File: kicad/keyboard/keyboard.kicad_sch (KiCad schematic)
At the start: 190 parts, among them J1 To main board J1, SW100 Esc, SW101 1 !, SW102 2 @, SW103 3 #, SW104 4 $, SW105 5 %, SW106 6 ^, SW107 7 &, SW110 8 *, SW111 9 (, SW112 0 ), SW113 - _, SW114 = +, SW115 Bksp, SW116 Tab, SW117 Q, SW120 W, SW121 E, SW122 R, SW123 T, SW124 Y, SW125 U, SW126 I, SW127 O, SW130 P, SW131 [ {, SW132 ] }, SW133 \ |, SW134 LCtrl, SW135 A, SW136 S, SW137 D, SW140 F, SW141 G, SW142 H, SW143 J, SW144 K, SW145 L, SW146 ; :, SW147 ' ", SW150 Enter, SW151 LShift, SW152 Z, SW153 X, SW154 C, SW155 V, SW156 B, SW157 N, SW160 M, SW161 , <, SW162 . >, SW163 / ?, SW164 RShift, SW165 Up, SW166 Caps, SW167 Fn, SW170 RAlt, SW171 LAlt, SW172 Space, SW173 RCtrl, SW175 Left, SW176 Down, SW177 Right

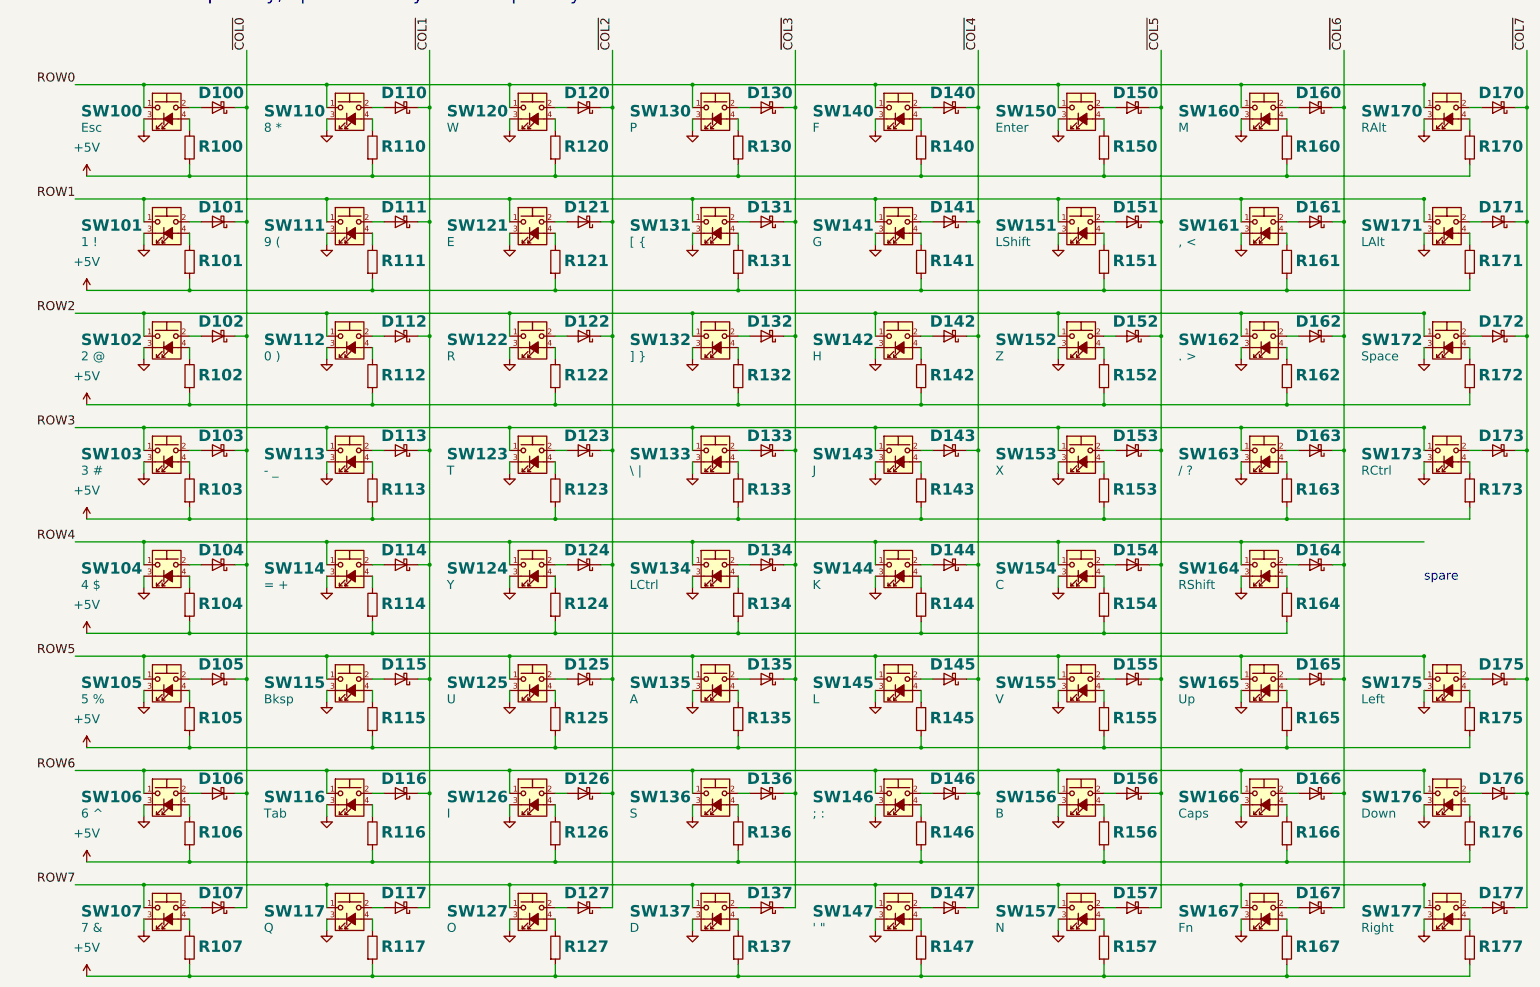
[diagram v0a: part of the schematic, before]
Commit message: Number parts from 1 for each kind; US zigzag resistor symbols
Main board R1-R54, RN1-RN2, D1-D5, JP1-JP2, F1, NT1, non-decoupling
capacitors C41-C46 (decaps keep Cn = Un); keyboard keys 1-63 row by row
(SWn, Dn, Rn per key). Resistors use R_US / R_Network08_US. --check now
fails on gaps or hundreds in the numbering. PDFs regenerated.

Co-Authored-By: Claude Opus 5.5 (1M context) <noreply@anthropic.com>
Claude-Session: https://claude.ai/code/session_01L9AkLuEg13EebxDmgXsaEp
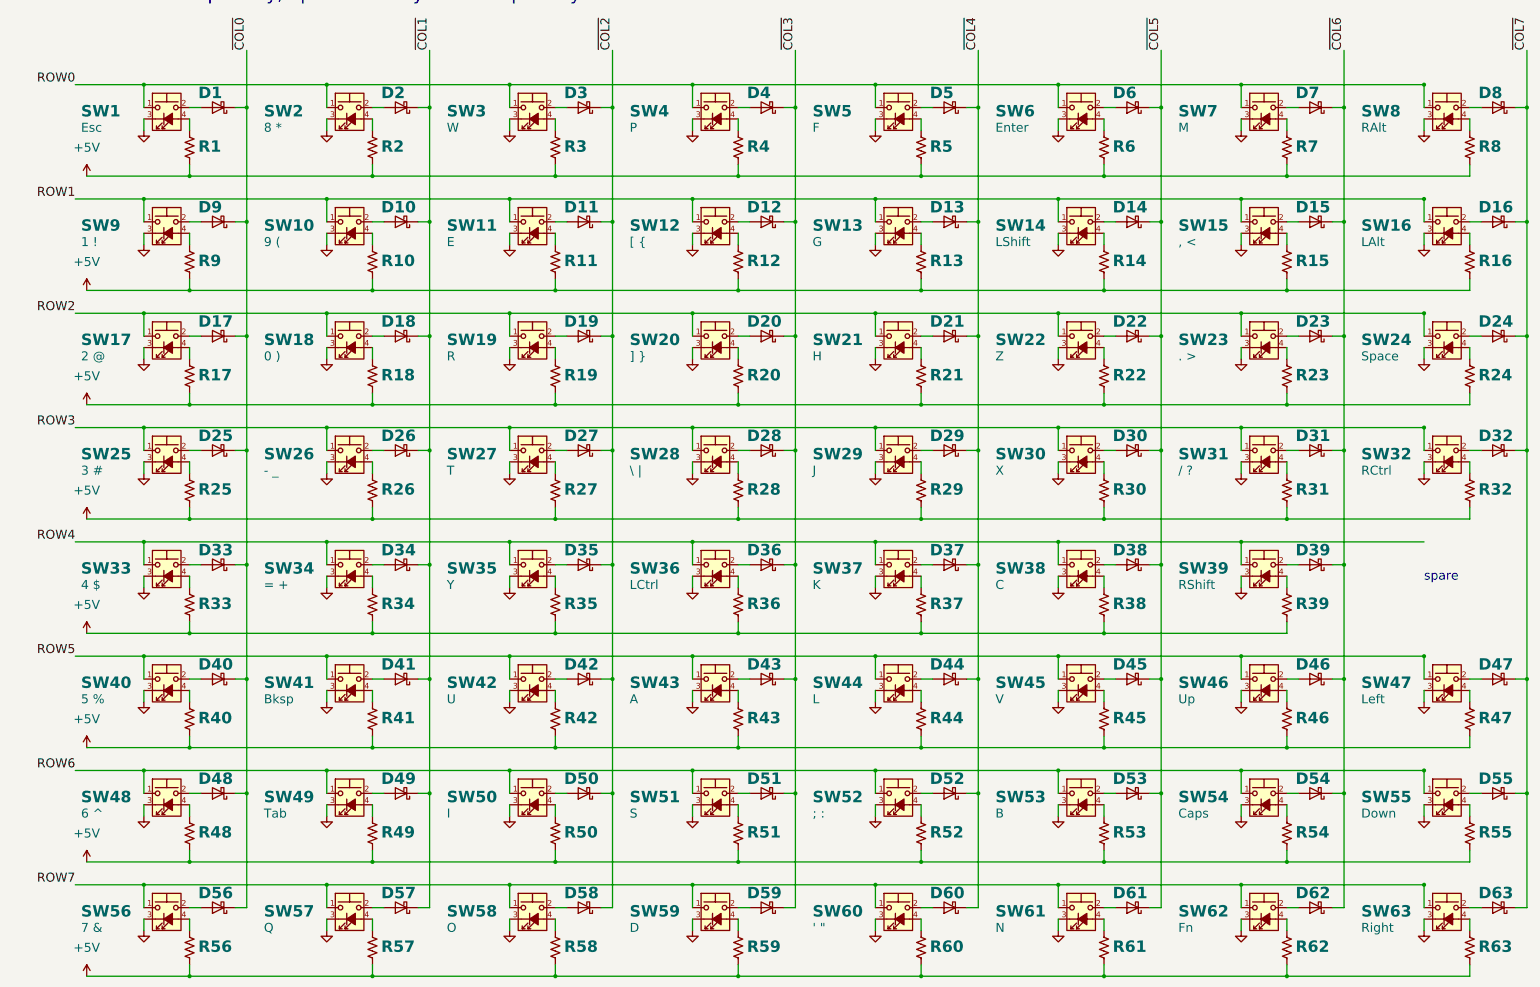
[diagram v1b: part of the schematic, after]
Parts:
- removed D100, D101, D102, D103, D104, D105, D106, D107, D110, D111, D112, D113, D114, D115, D116, D117, D120, D121, D122, D123, D124, D125, D126, D127, D130, D131, D132, D133, D134, D135, D136, D137, D140, D141, D142, D143, D144, D145, D146, D147, D150, D151, D152, D153, D154, D155, D156, D157, D160, D161, D162, D163, D164, D165, D166, D167, D170, D171, D172, D173, D175, D176, D177: BAT85, Diode_THT:D_DO-35_SOD27_P7.62mm_Horizontal, symbol placard_std:D_Schottky
- removed R100, R101, R102, R103, R104, R105, R106, R107, R110, R111, R112, R113, R114, R115, R116, R117, R120, R121, R122, R123, R124, R125, R126, R127, R130, R131, R132, R133, R134, R135, R136, R137, R140, R141, R142, R143, R144, R145, R146, R147, R150, R151, R152, R153, R154, R155, R156, R157, R160, R161, R162, R163, R164, R165, R166, R167, R170, R171, R172, R173, R175, R176, R177: 1k, Resistor_THT:R_Axial_DIN0207_L6.3mm_D2.5mm_P10.16mm_Horizontal, symbol placard_std:R
- removed SW100: Esc, placard:SW_Cherry_MX_LED_1.00u_PCB, symbol Switch:SW_Push_LED
- removed SW101: 1 !, placard:SW_Cherry_MX_LED_1.00u_PCB, symbol Switch:SW_Push_LED
- removed SW102: 2 @, placard:SW_Cherry_MX_LED_1.00u_PCB, symbol Switch:SW_Push_LED
- removed SW103: 3 #, placard:SW_Cherry_MX_LED_1.00u_PCB, symbol Switch:SW_Push_LED
- removed SW104: 4 $, placard:SW_Cherry_MX_LED_1.00u_PCB, symbol Switch:SW_Push_LED
- removed SW105: 5 %, placard:SW_Cherry_MX_LED_1.00u_PCB, symbol Switch:SW_Push_LED
- removed SW106: 6 ^, placard:SW_Cherry_MX_LED_1.00u_PCB, symbol Switch:SW_Push_LED
- removed SW107: 7 &, placard:SW_Cherry_MX_LED_1.00u_PCB, symbol Switch:SW_Push_LED
- removed SW110: 8 *, placard:SW_Cherry_MX_LED_1.00u_PCB, symbol Switch:SW_Push_LED
- removed SW111: 9 (, placard:SW_Cherry_MX_LED_1.00u_PCB, symbol Switch:SW_Push_LED
- removed SW112: 0 ), placard:SW_Cherry_MX_LED_1.00u_PCB, symbol Switch:SW_Push_LED
- removed SW113: - _, placard:SW_Cherry_MX_LED_1.00u_PCB, symbol Switch:SW_Push_LED
- removed SW114: = +, placard:SW_Cherry_MX_LED_1.00u_PCB, symbol Switch:SW_Push_LED
- removed SW115: Bksp, placard:SW_Cherry_MX_LED_2.00u_PCB, symbol Switch:SW_Push_LED
- removed SW116: Tab, placard:SW_Cherry_MX_LED_1.50u_PCB, symbol Switch:SW_Push_LED
- removed SW117: Q, placard:SW_Cherry_MX_LED_1.00u_PCB, symbol Switch:SW_Push_LED
- removed SW120: W, placard:SW_Cherry_MX_LED_1.00u_PCB, symbol Switch:SW_Push_LED
- removed SW121: E, placard:SW_Cherry_MX_LED_1.00u_PCB, symbol Switch:SW_Push_LED
- removed SW122: R, placard:SW_Cherry_MX_LED_1.00u_PCB, symbol Switch:SW_Push_LED
- removed SW123: T, placard:SW_Cherry_MX_LED_1.00u_PCB, symbol Switch:SW_Push_LED
- removed SW124: Y, placard:SW_Cherry_MX_LED_1.00u_PCB, symbol Switch:SW_Push_LED
- removed SW125: U, placard:SW_Cherry_MX_LED_1.00u_PCB, symbol Switch:SW_Push_LED
- removed SW126: I, placard:SW_Cherry_MX_LED_1.00u_PCB, symbol Switch:SW_Push_LED
- removed SW127: O, placard:SW_Cherry_MX_LED_1.00u_PCB, symbol Switch:SW_Push_LED
- removed SW130: P, placard:SW_Cherry_MX_LED_1.00u_PCB, symbol Switch:SW_Push_LED
- removed SW131: [ {, placard:SW_Cherry_MX_LED_1.00u_PCB, symbol Switch:SW_Push_LED
- removed SW132: ] }, placard:SW_Cherry_MX_LED_1.00u_PCB, symbol Switch:SW_Push_LED
- removed SW133: \ |, placard:SW_Cherry_MX_LED_1.50u_PCB, symbol Switch:SW_Push_LED
- removed SW134: LCtrl, placard:SW_Cherry_MX_LED_1.25u_PCB, symbol Switch:SW_Push_LED
- removed SW135: A, placard:SW_Cherry_MX_LED_1.00u_PCB, symbol Switch:SW_Push_LED
- removed SW136: S, placard:SW_Cherry_MX_LED_1.00u_PCB, symbol Switch:SW_Push_LED
- removed SW137: D, placard:SW_Cherry_MX_LED_1.00u_PCB, symbol Switch:SW_Push_LED
- removed SW140: F, placard:SW_Cherry_MX_LED_1.00u_PCB, symbol Switch:SW_Push_LED
- removed SW141: G, placard:SW_Cherry_MX_LED_1.00u_PCB, symbol Switch:SW_Push_LED
- removed SW142: H, placard:SW_Cherry_MX_LED_1.00u_PCB, symbol Switch:SW_Push_LED
- removed SW143: J, placard:SW_Cherry_MX_LED_1.00u_PCB, symbol Switch:SW_Push_LED
- removed SW144: K, placard:SW_Cherry_MX_LED_1.00u_PCB, symbol Switch:SW_Push_LED
- removed SW145: L, placard:SW_Cherry_MX_LED_1.00u_PCB, symbol Switch:SW_Push_LED
- removed SW146: ; :, placard:SW_Cherry_MX_LED_1.00u_PCB, symbol Switch:SW_Push_LED
- removed SW147: ' ", placard:SW_Cherry_MX_LED_1.00u_PCB, symbol Switch:SW_Push_LED
- removed SW150: Enter, placard:SW_Cherry_MX_LED_2.25u_PCB, symbol Switch:SW_Push_LED
- removed SW151: LShift, placard:SW_Cherry_MX_LED_2.25u_PCB, symbol Switch:SW_Push_LED
- removed SW152: Z, placard:SW_Cherry_MX_LED_1.00u_PCB, symbol Switch:SW_Push_LED
- removed SW153: X, placard:SW_Cherry_MX_LED_1.00u_PCB, symbol Switch:SW_Push_LED
- removed SW154: C, placard:SW_Cherry_MX_LED_1.00u_PCB, symbol Switch:SW_Push_LED
- removed SW155: V, placard:SW_Cherry_MX_LED_1.00u_PCB, symbol Switch:SW_Push_LED
- removed SW156: B, placard:SW_Cherry_MX_LED_1.00u_PCB, symbol Switch:SW_Push_LED
- removed SW157: N, placard:SW_Cherry_MX_LED_1.00u_PCB, symbol Switch:SW_Push_LED
- removed SW160: M, placard:SW_Cherry_MX_LED_1.00u_PCB, symbol Switch:SW_Push_LED
- removed SW161: , <, placard:SW_Cherry_MX_LED_1.00u_PCB, symbol Switch:SW_Push_LED
- removed SW162: . >, placard:SW_Cherry_MX_LED_1.00u_PCB, symbol Switch:SW_Push_LED
- removed SW163: / ?, placard:SW_Cherry_MX_LED_1.00u_PCB, symbol Switch:SW_Push_LED
- removed SW164: RShift, placard:SW_Cherry_MX_LED_1.75u_PCB, symbol Switch:SW_Push_LED
- removed SW165: Up, placard:SW_Cherry_MX_LED_1.00u_PCB, symbol Switch:SW_Push_LED
- removed SW166: Caps, placard:SW_Cherry_MX_LED_1.75u_PCB, symbol Switch:SW_Push_LED
- removed SW167: Fn, placard:SW_Cherry_MX_LED_1.25u_PCB, symbol Switch:SW_Push_LED
- removed SW170: RAlt, placard:SW_Cherry_MX_LED_1.00u_PCB, symbol Switch:SW_Push_LED
- removed SW171: LAlt, placard:SW_Cherry_MX_LED_1.25u_PCB, symbol Switch:SW_Push_LED
- removed SW172: Space, placard:SW_Cherry_MX_LED_6.25u_PCB, symbol Switch:SW_Push_LED
- removed SW173: RCtrl, placard:SW_Cherry_MX_LED_1.00u_PCB, symbol Switch:SW_Push_LED
- removed SW175: Left, placard:SW_Cherry_MX_LED_1.00u_PCB, symbol Switch:SW_Push_LED
- removed SW176: Down, placard:SW_Cherry_MX_LED_1.00u_PCB, symbol Switch:SW_Push_LED
- removed SW177: Right, placard:SW_Cherry_MX_LED_1.00u_PCB, symbol Switch:SW_Push_LED
- added D1, D10, D11, D12, D13, D14, D15, D16, D17, D18, D19, D2, D20, D21, D22, D23, D24, D25, D26, D27, D28, D29, D3, D30, D31, D32, D33, D34, D35, D36, D37, D38, D39, D4, D40, D41, D42, D43, D44, D45, D46, D47, D48, D49, D5, D50, D51, D52, D53, D54, D55, D56, D57, D58, D59, D6, D60, D61, D62, D63, D7, D8, D9: BAT85, Diode_THT:D_DO-35_SOD27_P7.62mm_Horizontal, symbol placard_std:D_Schottky
- added R1, R10, R11, R12, R13, R14, R15, R16, R17, R18, R19, R2, R20, R21, R22, R23, R24, R25, R26, R27, R28, R29, R3, R30, R31, R32, R33, R34, R35, R36, R37, R38, R39, R4, R40, R41, R42, R43, R44, R45, R46, R47, R48, R49, R5, R50, R51, R52, R53, R54, R55, R56, R57, R58, R59, R6, R60, R61, R62, R63, R7, R8, R9: 1k, Resistor_THT:R_Axial_DIN0207_L6.3mm_D2.5mm_P10.16mm_Horizontal, symbol placard_std:R_US
- added SW1: Esc, placard:SW_Cherry_MX_LED_1.00u_PCB, symbol Switch:SW_Push_LED
- added SW10: 9 (, placard:SW_Cherry_MX_LED_1.00u_PCB, symbol Switch:SW_Push_LED
- added SW11: E, placard:SW_Cherry_MX_LED_1.00u_PCB, symbol Switch:SW_Push_LED
- added SW12: [ {, placard:SW_Cherry_MX_LED_1.00u_PCB, symbol Switch:SW_Push_LED
- added SW13: G, placard:SW_Cherry_MX_LED_1.00u_PCB, symbol Switch:SW_Push_LED
- added SW14: LShift, placard:SW_Cherry_MX_LED_2.25u_PCB, symbol Switch:SW_Push_LED
- added SW15: , <, placard:SW_Cherry_MX_LED_1.00u_PCB, symbol Switch:SW_Push_LED
- added SW16: LAlt, placard:SW_Cherry_MX_LED_1.25u_PCB, symbol Switch:SW_Push_LED
- added SW17: 2 @, placard:SW_Cherry_MX_LED_1.00u_PCB, symbol Switch:SW_Push_LED
- added SW18: 0 ), placard:SW_Cherry_MX_LED_1.00u_PCB, symbol Switch:SW_Push_LED
- added SW19: R, placard:SW_Cherry_MX_LED_1.00u_PCB, symbol Switch:SW_Push_LED
- added SW2: 8 *, placard:SW_Cherry_MX_LED_1.00u_PCB, symbol Switch:SW_Push_LED
- added SW20: ] }, placard:SW_Cherry_MX_LED_1.00u_PCB, symbol Switch:SW_Push_LED
- added SW21: H, placard:SW_Cherry_MX_LED_1.00u_PCB, symbol Switch:SW_Push_LED
- added SW22: Z, placard:SW_Cherry_MX_LED_1.00u_PCB, symbol Switch:SW_Push_LED
- added SW23: . >, placard:SW_Cherry_MX_LED_1.00u_PCB, symbol Switch:SW_Push_LED
- added SW24: Space, placard:SW_Cherry_MX_LED_6.25u_PCB, symbol Switch:SW_Push_LED
- added SW25: 3 #, placard:SW_Cherry_MX_LED_1.00u_PCB, symbol Switch:SW_Push_LED
- added SW26: - _, placard:SW_Cherry_MX_LED_1.00u_PCB, symbol Switch:SW_Push_LED
- added SW27: T, placard:SW_Cherry_MX_LED_1.00u_PCB, symbol Switch:SW_Push_LED
- added SW28: \ |, placard:SW_Cherry_MX_LED_1.50u_PCB, symbol Switch:SW_Push_LED
- added SW29: J, placard:SW_Cherry_MX_LED_1.00u_PCB, symbol Switch:SW_Push_LED
- added SW3: W, placard:SW_Cherry_MX_LED_1.00u_PCB, symbol Switch:SW_Push_LED
- added SW30: X, placard:SW_Cherry_MX_LED_1.00u_PCB, symbol Switch:SW_Push_LED
- added SW31: / ?, placard:SW_Cherry_MX_LED_1.00u_PCB, symbol Switch:SW_Push_LED
- added SW32: RCtrl, placard:SW_Cherry_MX_LED_1.00u_PCB, symbol Switch:SW_Push_LED
- added SW33: 4 $, placard:SW_Cherry_MX_LED_1.00u_PCB, symbol Switch:SW_Push_LED
- added SW34: = +, placard:SW_Cherry_MX_LED_1.00u_PCB, symbol Switch:SW_Push_LED
- added SW35: Y, placard:SW_Cherry_MX_LED_1.00u_PCB, symbol Switch:SW_Push_LED
- added SW36: LCtrl, placard:SW_Cherry_MX_LED_1.25u_PCB, symbol Switch:SW_Push_LED
- added SW37: K, placard:SW_Cherry_MX_LED_1.00u_PCB, symbol Switch:SW_Push_LED
- added SW38: C, placard:SW_Cherry_MX_LED_1.00u_PCB, symbol Switch:SW_Push_LED
- added SW39: RShift, placard:SW_Cherry_MX_LED_1.75u_PCB, symbol Switch:SW_Push_LED
- added SW4: P, placard:SW_Cherry_MX_LED_1.00u_PCB, symbol Switch:SW_Push_LED
- added SW40: 5 %, placard:SW_Cherry_MX_LED_1.00u_PCB, symbol Switch:SW_Push_LED
- added SW41: Bksp, placard:SW_Cherry_MX_LED_2.00u_PCB, symbol Switch:SW_Push_LED
- added SW42: U, placard:SW_Cherry_MX_LED_1.00u_PCB, symbol Switch:SW_Push_LED
- added SW43: A, placard:SW_Cherry_MX_LED_1.00u_PCB, symbol Switch:SW_Push_LED
- added SW44: L, placard:SW_Cherry_MX_LED_1.00u_PCB, symbol Switch:SW_Push_LED
- added SW45: V, placard:SW_Cherry_MX_LED_1.00u_PCB, symbol Switch:SW_Push_LED
- added SW46: Up, placard:SW_Cherry_MX_LED_1.00u_PCB, symbol Switch:SW_Push_LED
- added SW47: Left, placard:SW_Cherry_MX_LED_1.00u_PCB, symbol Switch:SW_Push_LED
- added SW48: 6 ^, placard:SW_Cherry_MX_LED_1.00u_PCB, symbol Switch:SW_Push_LED
- added SW49: Tab, placard:SW_Cherry_MX_LED_1.50u_PCB, symbol Switch:SW_Push_LED
- added SW5: F, placard:SW_Cherry_MX_LED_1.00u_PCB, symbol Switch:SW_Push_LED
- added SW50: I, placard:SW_Cherry_MX_LED_1.00u_PCB, symbol Switch:SW_Push_LED
- added SW51: S, placard:SW_Cherry_MX_LED_1.00u_PCB, symbol Switch:SW_Push_LED
- added SW52: ; :, placard:SW_Cherry_MX_LED_1.00u_PCB, symbol Switch:SW_Push_LED
- added SW53: B, placard:SW_Cherry_MX_LED_1.00u_PCB, symbol Switch:SW_Push_LED
- added SW54: Caps, placard:SW_Cherry_MX_LED_1.75u_PCB, symbol Switch:SW_Push_LED
- added SW55: Down, placard:SW_Cherry_MX_LED_1.00u_PCB, symbol Switch:SW_Push_LED
- added SW56: 7 &, placard:SW_Cherry_MX_LED_1.00u_PCB, symbol Switch:SW_Push_LED
- added SW57: Q, placard:SW_Cherry_MX_LED_1.00u_PCB, symbol Switch:SW_Push_LED
- added SW58: O, placard:SW_Cherry_MX_LED_1.00u_PCB, symbol Switch:SW_Push_LED
- added SW59: D, placard:SW_Cherry_MX_LED_1.00u_PCB, symbol Switch:SW_Push_LED
- added SW6: Enter, placard:SW_Cherry_MX_LED_2.25u_PCB, symbol Switch:SW_Push_LED
- added SW60: ' ", placard:SW_Cherry_MX_LED_1.00u_PCB, symbol Switch:SW_Push_LED
- added SW61: N, placard:SW_Cherry_MX_LED_1.00u_PCB, symbol Switch:SW_Push_LED
- added SW62: Fn, placard:SW_Cherry_MX_LED_1.25u_PCB, symbol Switch:SW_Push_LED
- added SW63: Right, placard:SW_Cherry_MX_LED_1.00u_PCB, symbol Switch:SW_Push_LED
- added SW7: M, placard:SW_Cherry_MX_LED_1.00u_PCB, symbol Switch:SW_Push_LED
- added SW8: RAlt, placard:SW_Cherry_MX_LED_1.00u_PCB, symbol Switch:SW_Push_LED
- added SW9: 1 !, placard:SW_Cherry_MX_LED_1.00u_PCB, symbol Switch:SW_Push_LED
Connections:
- net +5V: now also R1.2, R10.2, R11.2, R12.2, R13.2, R14.2, R15.2, R16.2, R17.2, R18.2, R19.2, R2.2, R20.2, R21.2, R22.2, R23.2, R24.2, R25.2, R26.2, R27.2, R28.2, R29.2, R3.2, R30.2, R31.2, R32.2, R33.2, R34.2, R35.2, R36.2, R37.2, R38.2, R39.2, R4.2, R40.2, R41.2, R42.2, R43.2, R44.2, R45.2, R46.2, R47.2, R48.2, R49.2, R5.2, R50.2, R51.2, R52.2, R53.2, R54.2, R55.2, R56.2, R57.2, R58.2, R59.2, R6.2, R60.2, R61.2, R62.2, R63.2, R7.2, R8.2, R9.2
- net GND: now also SW1.3 (K), SW10.3 (K), SW11.3 (K), SW12.3 (K), SW13.3 (K), SW14.3 (K), SW15.3 (K), SW16.3 (K), SW17.3 (K), SW18.3 (K), SW19.3 (K), SW2.3 (K), SW20.3 (K), SW21.3 (K), SW22.3 (K), SW23.3 (K), SW24.3 (K), SW25.3 (K), SW26.3 (K), SW27.3 (K), SW28.3 (K), SW29.3 (K), SW3.3 (K), SW30.3 (K), SW31.3 (K), SW32.3 (K), SW33.3 (K), SW34.3 (K), SW35.3 (K), SW36.3 (K), SW37.3 (K), SW38.3 (K), SW39.3 (K), SW4.3 (K), SW40.3 (K), SW41.3 (K), SW42.3 (K), SW43.3 (K), SW44.3 (K), SW45.3 (K), SW46.3 (K), SW47.3 (K), SW48.3 (K), SW49.3 (K), SW5.3 (K), SW50.3 (K), SW51.3 (K), SW52.3 (K), SW53.3 (K), SW54.3 (K), SW55.3 (K), SW56.3 (K), SW57.3 (K), SW58.3 (K), SW59.3 (K), SW6.3 (K), SW60.3 (K), SW61.3 (K), SW62.3 (K), SW63.3 (K), SW7.3 (K), SW8.3 (K), SW9.3 (K)
- net ROW0: now also SW1.1, SW2.1, SW3.1, SW4.1, SW5.1, SW6.1, SW7.1, SW8.1
- net ROW1: now also SW10.1, SW11.1, SW12.1, SW13.1, SW14.1, SW15.1, SW16.1, SW9.1
- net ROW2: now also SW17.1, SW18.1, SW19.1, SW20.1, SW21.1, SW22.1, SW23.1, SW24.1
- net ROW3: now also SW25.1, SW26.1, SW27.1, SW28.1, SW29.1, SW30.1, SW31.1, SW32.1
- net ROW4: now also SW33.1, SW34.1, SW35.1, SW36.1, SW37.1, SW38.1, SW39.1
- net ROW5: now also SW40.1, SW41.1, SW42.1, SW43.1, SW44.1, SW45.1, SW46.1, SW47.1
- net ROW6: now also SW48.1, SW49.1, SW50.1, SW51.1, SW52.1, SW53.1, SW54.1, SW55.1
- net ROW7: now also SW56.1, SW57.1, SW58.1, SW59.1, SW60.1, SW61.1, SW62.1, SW63.1
- net ~{COL0}: now also D1.1 (K), D17.1 (K), D25.1 (K), D33.1 (K), D40.1 (K), D48.1 (K), D56.1 (K), D9.1 (K)
- net ~{COL1}: now also D10.1 (K), D18.1 (K), D2.1 (K), D26.1 (K), D34.1 (K), D41.1 (K), D49.1 (K), D57.1 (K)
- net ~{COL2}: now also D11.1 (K), D19.1 (K), D27.1 (K), D3.1 (K), D35.1 (K), D42.1 (K), D50.1 (K), D58.1 (K)
- net ~{COL3}: now also D12.1 (K), D20.1 (K), D28.1 (K), D36.1 (K), D4.1 (K), D43.1 (K), D51.1 (K), D59.1 (K)
- net ~{COL4}: now also D13.1 (K), D21.1 (K), D29.1 (K), D37.1 (K), D44.1 (K), D5.1 (K), D52.1 (K), D60.1 (K)
- net ~{COL5}: now also D14.1 (K), D22.1 (K), D30.1 (K), D38.1 (K), D45.1 (K), D53.1 (K), D6.1 (K), D61.1 (K)
- net ~{COL6}: now also D15.1 (K), D23.1 (K), D31.1 (K), D39.1 (K), D46.1 (K), D54.1 (K), D62.1 (K), D7.1 (K)
- net ~{COL7}: now also D16.1 (K), D24.1 (K), D32.1 (K), D47.1 (K), D55.1 (K), D63.1 (K), D8.1 (K)
- new net: D35.2 (A), SW35.2
- new net: D22.2 (A), SW22.2
- new net: R22.1, SW22.4 (A)
- new net: R24.1, SW24.4 (A)
- new net: D48.2 (A), SW48.2
- new net: R48.1, SW48.4 (A)
- new net: D47.2 (A), SW47.2
- new net: R47.1, SW47.4 (A)
- new net: D29.2 (A), SW29.2
- new net: R29.1, SW29.4 (A)
- new net: R18.1, SW18.4 (A)
- new net: D8.2 (A), SW8.2
- new net: R8.1, SW8.4 (A)
- new net: D61.2 (A), SW61.2
- new net: R61.1, SW61.4 (A)
- new net: R31.1, SW31.4 (A)
- new net: R3.1, SW3.4 (A)
- new net: D11.2 (A), SW11.2
- new net: D30.2 (A), SW30.2
- new net: R30.1, SW30.4 (A)
- new net: D39.2 (A), SW39.2
- new net: D26.2 (A), SW26.2
- new net: R26.1, SW26.4 (A)
- new net: D56.2 (A), SW56.2
- new net: R16.1, SW16.4 (A)
- new net: R58.1, SW58.4 (A)
- new net: R12.1, SW12.4 (A)
- new net: R33.1, SW33.4 (A)
- new net: D33.2 (A), SW33.2
- new net: D58.2 (A), SW58.2
- new net: D2.2 (A), SW2.2
- new net: R2.1, SW2.4 (A)
- new net: D40.2 (A), SW40.2
- new net: D5.2 (A), SW5.2
- new net: R5.1, SW5.4 (A)
- new net: R62.1, SW62.4 (A)
- new net: R40.1, SW40.4 (A)
- new net: R39.1, SW39.4 (A)
- new net: D16.2 (A), SW16.2
- new net: D54.2 (A), SW54.2
- new net: D20.2 (A), SW20.2
- new net: D32.2 (A), SW32.2
- new net: R32.1, SW32.4 (A)
- new net: D7.2 (A), SW7.2
- new net: R7.1, SW7.4 (A)
- new net: D59.2 (A), SW59.2
- new net: D23.2 (A), SW23.2
- new net: D25.2 (A), SW25.2
- new net: R25.1, SW25.4 (A)
- new net: D37.2 (A), SW37.2
- new net: R37.1, SW37.4 (A)
- new net: R46.1, SW46.4 (A)
- new net: D9.2 (A), SW9.2
- new net: R9.1, SW9.4 (A)
- new net: R54.1, SW54.4 (A)
- new net: D63.2 (A), SW63.2
- new net: R63.1, SW63.4 (A)
- new net: D43.2 (A), SW43.2
- new net: R43.1, SW43.4 (A)
- new net: D27.2 (A), SW27.2
- new net: R27.1, SW27.4 (A)
- new net: D42.2 (A), SW42.2
- new net: R42.1, SW42.4 (A)
- new net: D57.2 (A), SW57.2
- new net: R57.1, SW57.4 (A)
- new net: R59.1, SW59.4 (A)
- new net: R56.1, SW56.4 (A)
- new net: R21.1, SW21.4 (A)
- new net: D21.2 (A), SW21.2
- new net: R11.1, SW11.4 (A)
- new net: D15.2 (A), SW15.2
- new net: D13.2 (A), SW13.2
- new net: D60.2 (A), SW60.2
- new net: D28.2 (A), SW28.2
- new net: D46.2 (A), SW46.2
- new net: R35.1, SW35.4 (A)
- new net: D14.2 (A), SW14.2
- new net: R36.1, SW36.4 (A)
- new net: D6.2 (A), SW6.2
- new net: R6.1, SW6.4 (A)
- new net: R52.1, SW52.4 (A)
- new net: D52.2 (A), SW52.2
- new net: D44.2 (A), SW44.2
- new net: R13.1, SW13.4 (A)
- new net: D4.2 (A), SW4.2
- new net: R4.1, SW4.4 (A)
- new net: R55.1, SW55.4 (A)
- new net: D10.2 (A), SW10.2
- new net: R10.1, SW10.4 (A)
- new net: R45.1, SW45.4 (A)
- new net: R50.1, SW50.4 (A)
- new net: D19.2 (A), SW19.2
- new net: R1.1, SW1.4 (A)
- new net: D34.2 (A), SW34.2
- new net: R41.1, SW41.4 (A)
- new net: R19.1, SW19.4 (A)
- new net: R51.1, SW51.4 (A)
- new net: D1.2 (A), SW1.2
- new net: D18.2 (A), SW18.2
- new net: D31.2 (A), SW31.2
- new net: D62.2 (A), SW62.2
- new net: R34.1, SW34.4 (A)
- new net: D41.2 (A), SW41.2
- new net: R60.1, SW60.4 (A)
- new net: D53.2 (A), SW53.2
- new net: R53.1, SW53.4 (A)
- new net: R28.1, SW28.4 (A)
- new net: R15.1, SW15.4 (A)
- new net: D38.2 (A), SW38.2
- new net: D24.2 (A), SW24.2
- new net: R44.1, SW44.4 (A)
- new net: D55.2 (A), SW55.2
- new net: D3.2 (A), SW3.2
- new net: D49.2 (A), SW49.2
- new net: R49.1, SW49.4 (A)
- new net: R23.1, SW23.4 (A)
- new net: R14.1, SW14.4 (A)
- new net: D17.2 (A), SW17.2
- new net: R20.1, SW20.4 (A)
- new net: D12.2 (A), SW12.2
- new net: D50.2 (A), SW50.2
- new net: D36.2 (A), SW36.2
- new net: D51.2 (A), SW51.2
- new net: R17.1, SW17.4 (A)
- new net: R38.1, SW38.4 (A)
- new net: D45.2 (A), SW45.2

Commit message: Bill of materials for the main board, cartridge and keyboard
Manufacturer and MPN fields on every schematic part (empty where none is
chosen), set from an MPN table in gen_kicad_schematic.py; net tie, cartridge
edge fingers and solder jumper excluded from the BOM.  gen_bom.py groups the
parts by part number into docs/BOM.md and docs/BOM.csv, adding sockets,
shunts, keyboard LEDs, keycaps, stabilizers and the keyboard ribbon cable.

Co-Authored-By: Claude Opus 5.5 (1M context) <noreply@anthropic.com>
Claude-Session: https://claude.ai/code/session_018iEnPngycbxX6Tt4Wzp3zN
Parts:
- D1, D10, D11, D12, D13, D14, D15, D16, D17, D18, D19, D2, D20, D21, D22, D23, D24, D25, D26, D27, D28, D29, D3, D30, D31, D32, D33, D34, D35, D36, D37, D38, D39, D4, D40, D41, D42, D43, D44, D45, D46, D47, D48, D49, D5, D50, D51, D52, D53, D54, D55, D56, D57, D58, D59, D6, D60, D61, D62, D63, D7, D8, D9: MPN (none) -> BAT85; Manufacturer (none) -> Vishay

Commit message: Part numbers for the remaining parts; J6 Tensility 54-00174; optional J1 and J9-J12
Every schematic part gets Manufacturer/MPN: Yageo MFR-25 resistors by value,
Bourns 4609X networks, KEMET/TDK ceramics, Panasonic FR electrolytics, ECS
oscillator, Assmann VGA, Sullins headers, Wurth box header, Cherry switches.
Sockets get On Shore numbers (0.3" 24/28-pin are ED241DT/ED281DT; ED28DT is
0.6"). J6 becomes the Tensility 54-00174 TRRS jack with a footprint drawn
from its datasheet. Digi-Key prices from Justin for the oscillator, VGA and
audio jack. The expansion slot sockets and the keyboard header are optional,
with a BOM total without them.

Co-Authored-By: Claude Opus 5.5 (1M context) <noreply@anthropic.com>
Claude-Session: https://claude.ai/code/session_01L9AkLuEg13EebxDmgXsaEp
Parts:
- J1: MPN (none) -> 61202021621; Manufacturer (none) -> Wurth Elektronik
- R1, R10, R11, R12, R13, R14, R15, R16, R17, R18, R19, R2, R20, R21, R22, R23, R24, R25, R26, R27, R28, R29, R3, R30, R31, R32, R33, R34, R35, R36, R37, R38, R39, R4, R40, R41, R42, R43, R44, R45, R46, R47, R48, R49, R5, R50, R51, R52, R53, R54, R55, R56, R57, R58, R59, R6, R60, R61, R62, R63, R7, R8, R9: MPN (none) -> MFR-25FBF52-1K; Manufacturer (none) -> Yageo
- SW1, SW10, SW11, SW12, SW13, SW14, SW15, SW16, SW17, SW18, SW19, SW2, SW20, SW21, SW22, SW23, SW24, SW25, SW26, SW27, SW28, SW29, SW3, SW30, SW31, SW32, SW33, SW34, SW35, SW36, SW37, SW38, SW39, SW4, SW40, SW41, SW42, SW43, SW44, SW45, SW46, SW47, SW48, SW49, SW5, SW50, SW51, SW52, SW53, SW54, SW55, SW56, SW57, SW58, SW59, SW6, SW60, SW61, SW62, SW63, SW7, SW8, SW9: MPN (none) -> MX2A-L1NB; Manufacturer (none) -> Cherry

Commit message: Kit footprints: DIP sockets with puller room and part number, resistors with value
Justin: put the chip-puller room in the socket footprints (User.Eco1,
2.5 mm past each end) and the part number in silkscreen between the pin
rows; resistors get their value in silkscreen on the body. New
gen_kicad_kit_footprints.py derives them from KiCad's stock footprints;
schematic, symbols, BOM and PDFs now name them. The board file is left
as is (Justin is editing it): Update PCB from Schematic swaps them in.

Co-Authored-By: Claude Opus 5.5 (1M context) <noreply@anthropic.com>
Claude-Session: https://claude.ai/code/session_01JnVuvUvdWezUUU6Sgmg16H
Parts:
- R1, R10, R11, R12, R13, R14, R15, R16, R17, R18, R19, R2, R20, R21, R22, R23, R24, R25, R26, R27, R28, R29, R3, R30, R31, R32, R33, R34, R35, R36, R37, R38, R39, R4, R40, R41, R42, R43, R44, R45, R46, R47, R48, R49, R5, R50, R51, R52, R53, R54, R55, R56, R57, R58, R59, R6, R60, R61, R62, R63, R7, R8, R9: footprint Resistor_THT:R_Axial_DIN0207_L6.3mm_D2.5mm_P10.16mm_Horizontal -> placard:R_Axial_DIN0207_L6.3mm_D2.5mm_P10.16mm_Horizontal_Value
